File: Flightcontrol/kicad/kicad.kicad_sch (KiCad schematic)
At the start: 3 parts, among them U1 ESP32-S3-WROOM-1U-N16R8

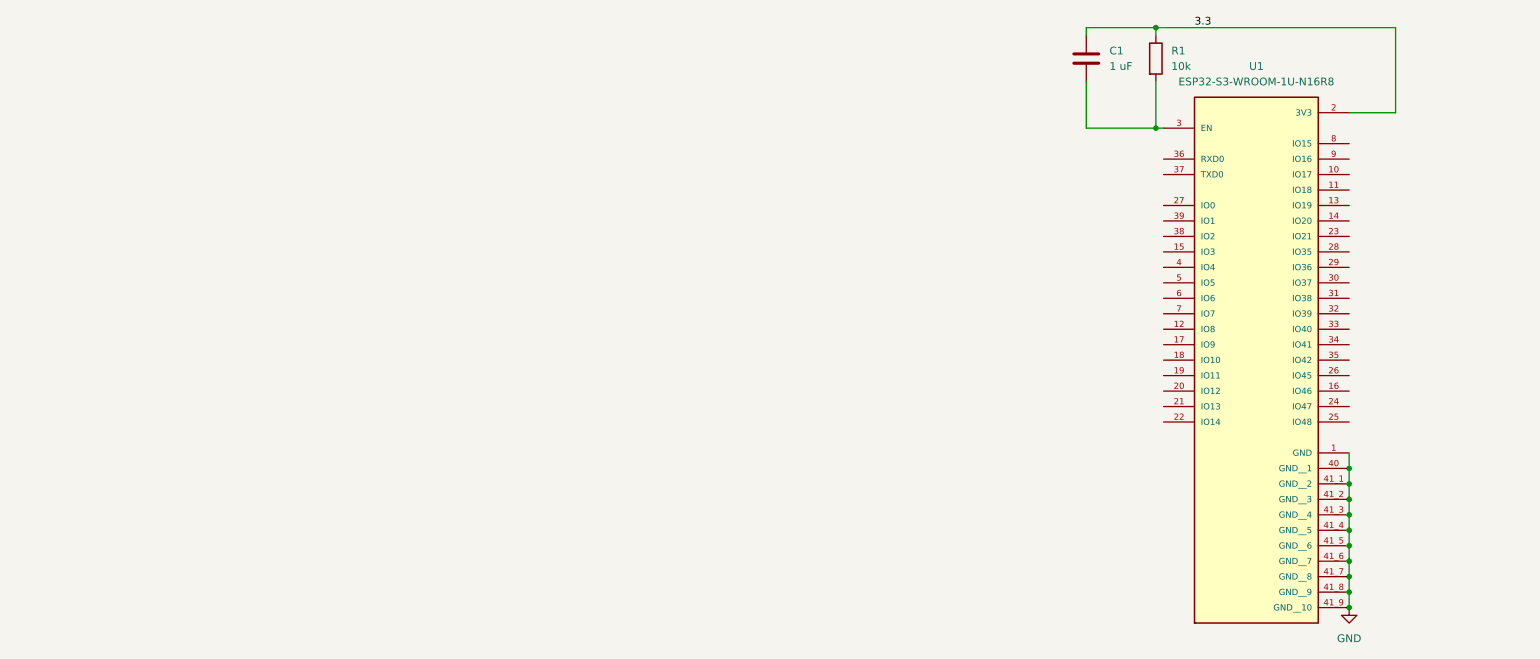
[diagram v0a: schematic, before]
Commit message: begun usbc programmer
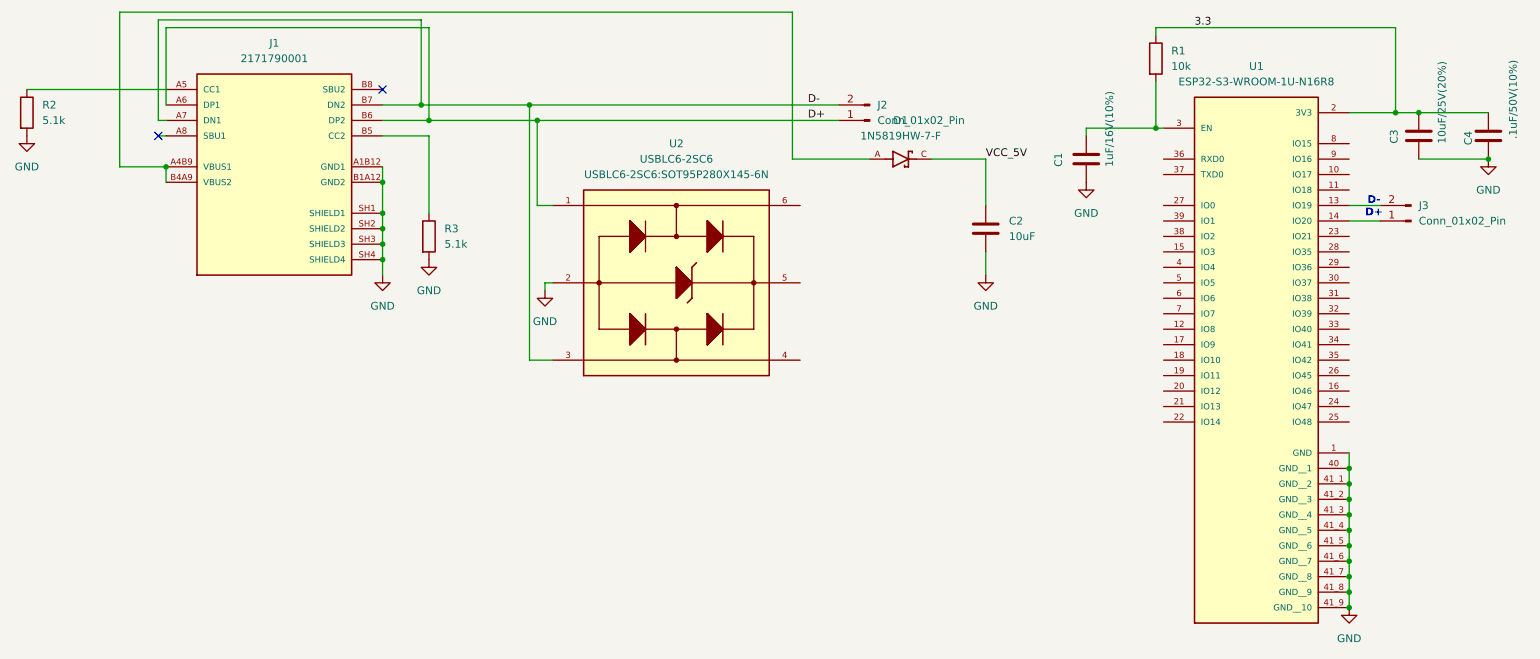
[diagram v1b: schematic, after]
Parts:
- added C2: 10uF, symbol Device:C
- added C3: 10uF/25V(20%), symbol Device:C
- added C4: .1uF/50V(10%), symbol Device:C
- added D1: 1N5819HW-7-F, 1N5819HW-7-F:SOD3715X145N, symbol 1N5819HW-7-F:1N5819HW-7-F
- added J1: 2171790001, 2171790001:MOLEX_2171790001, symbol 2171790001:2171790001
- added J2, J3: Conn_01x02_Pin, Connector_PinHeader_2.54mm:PinHeader_1x02_P2.54mm_Vertical, symbol Connector:Conn_01x02_Pin
- added R2, R3: 5.1k, symbol Device:R
- added U2: USBLC6-2SC6, USBLC6-2SC6:SOT95P280X145-6N, symbol USBLC6-2SC6:USBLC6-2SC6
- C1: value 1 uF -> 1uF/16V(10%)
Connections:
- net 3.3: now also C3.1, C4.1; no longer C1.1
- net GND: now also C1.2, C2.2, C3.2, C4.2, J1.A1B12 (GND1), J1.B1A12 (GND2), J1.SH1 (SHIELD1), J1.SH2 (SHIELD2), J1.SH3 (SHIELD3), J1.SH4 (SHIELD4), R2.2, R3.2, U2.2
- net at R1.2, U1.3 (EN): now also C1.1; no longer C1.2
- net at U1.13 (IO19): now also J3.2 (Pin_2)
- net at U1.14 (IO20): now also J3.1 (Pin_1)
- new net: D1.A, J1.A4B9 (VBUS1), J1.B4A9 (VBUS2)
- new net: J1.A5 (CC1), R2.1
- new net: J1.B5 (CC2), R3.1
- new net D+: J1.A6 (DP1), J1.B6 (DP2), J2.1 (Pin_1), U2.1
- new net D-: J1.A7 (DN1), J1.B7 (DN2), J2.2 (Pin_2), U2.3
- new net VCC_5V: C2.1, D1.C
- no-connect marks 0 -> 2
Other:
- note added: "D- D+"
- moved on the sheet: C1
